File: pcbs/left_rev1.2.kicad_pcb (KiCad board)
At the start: 2 copper layers, 101 x 79 mm, 31 parts

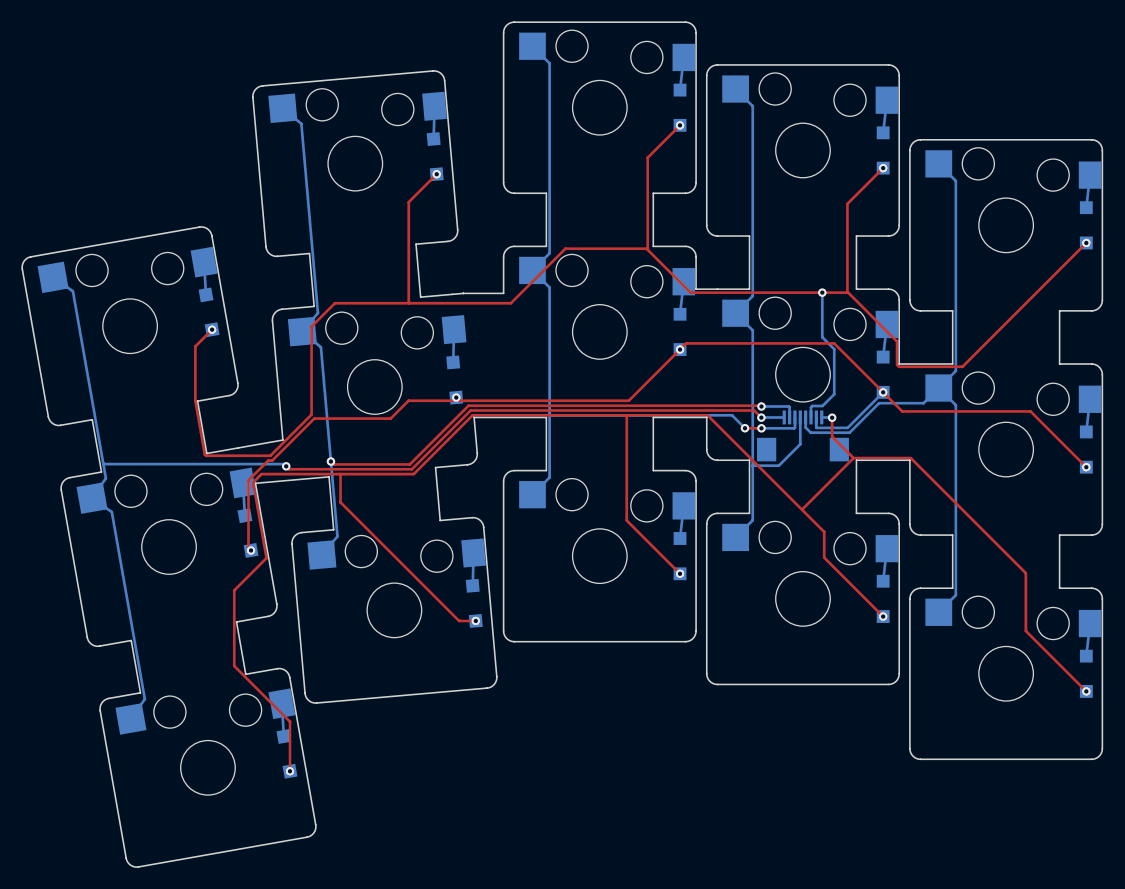
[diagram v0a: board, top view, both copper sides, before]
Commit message: Revision 1.2 - Socket was moved from middle home to inner home - Vertical column connections became thinner
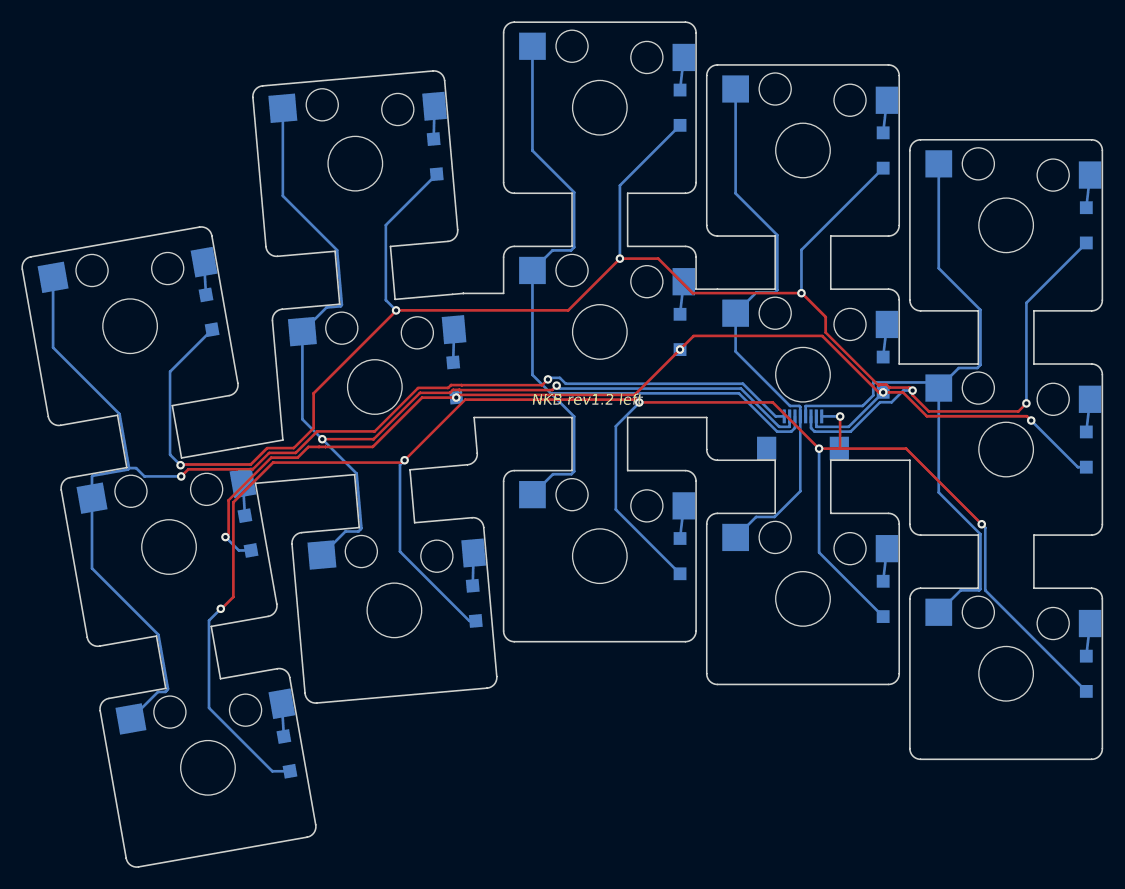
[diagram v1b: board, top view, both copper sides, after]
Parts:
- removed _6: , HKWClamshellSocket
- added _1: , HKWClamshellSocket, B.Cu at (159.3, 90.8)
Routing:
- net RL1: track 171.0 -> 185.6 mm
- net C2: track 90.9 -> 98.8 mm
- net C1: track 111.1 -> 118.2 mm
- net C3: track 69.1 -> 76.0 mm, vias 2 -> 0
- net C5: track 59.9 -> 65.7 mm
- net RL3: track 184.4 -> 189.6 mm
- net RL2: track 103.9 -> 106.7 mm
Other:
- outline, holes or cut-outs redrawn
- board text added: "NKB rev1.2 left"

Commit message: Some routing "art" for left side
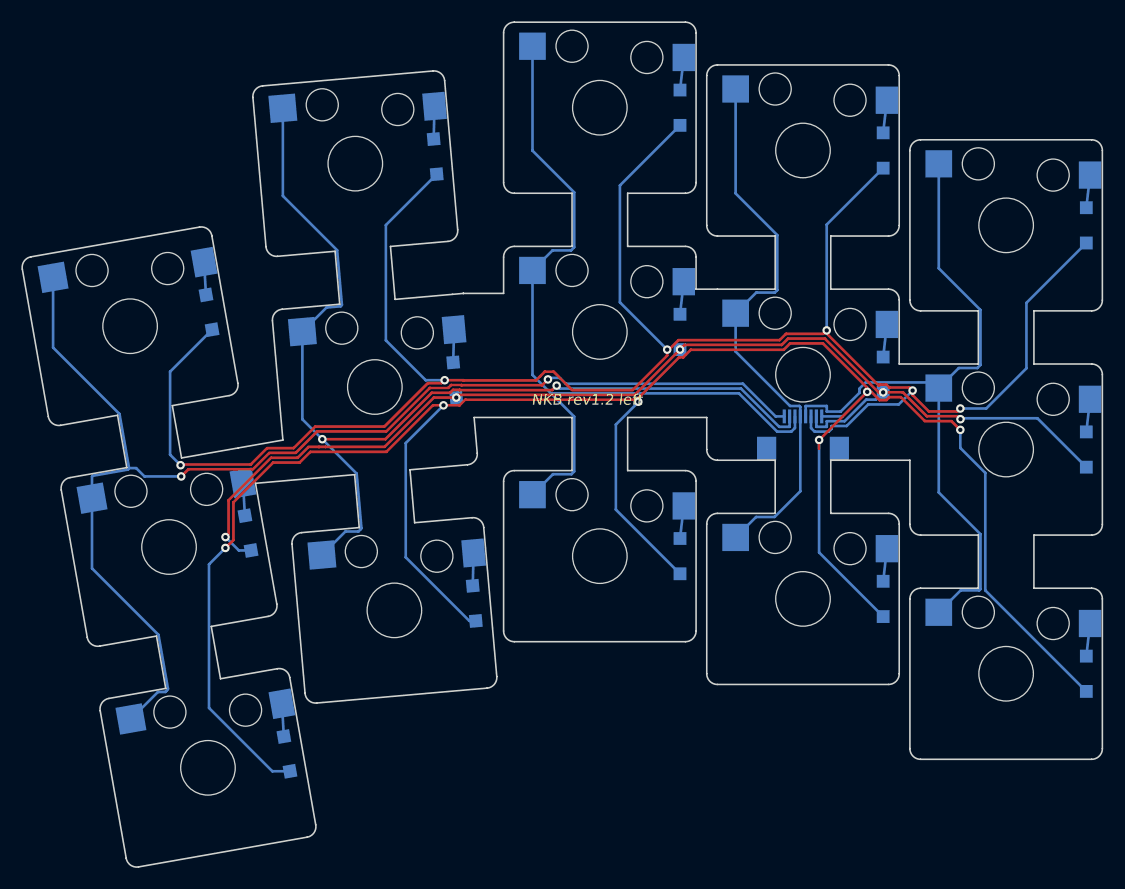
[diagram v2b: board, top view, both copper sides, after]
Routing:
- net RL3: track 189.6 -> 213.4 mm
- net RL1: track 185.6 -> 199.7 mm
